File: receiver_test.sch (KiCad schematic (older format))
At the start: 9 parts, among them J1 Conn_Coaxial, J2 Conn_Coaxial, J3 Conn_01x02_Male, J4 Conn_01x02_Male, J5 Conn_01x02_Male, U1 ADE-1H+

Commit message: Nyáktervezésre majdnem kész
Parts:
- added C33: 47u, Capacitor_SMD:CP_Elec_6.3x5.3, symbol Device:CP
- added C34: 100n, Capacitor_SMD:C_0805_2012Metric_Pad1.15x1.40mm_HandSolder, symbol Device:C
- added J6: Conn_01x02_Male, Connector_PinSocket_2.54mm:PinSocket_1x02_P2.54mm_Vertical, symbol Connector:Conn_01x02_Male
- added R11: 100, Resistor_SMD:R_0805_2012Metric_Pad1.15x1.40mm_HandSolder, symbol Device:R
- added R25, R26, R27, R28, R29, R30, R31, R32, R33, R34: BP, Resistor_SMD:R_1206_3216Metric_Pad1.42x1.75mm_HandSolder, symbol Device:R
- J2: footprint (none) -> Connector_Coaxial:SMA_Molex_73251-1153_EdgeMount_Horizontal
- J3, J4, J5: footprint (none) -> Connector_PinSocket_2.54mm:PinSocket_1x02_P2.54mm_Vertical
- R1, R2, R3: footprint (none) -> Resistor_SMD:R_0805_2012Metric_Pad1.15x1.40mm_HandSolder
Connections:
- net +5VA: now also C33.1, C34.1, R11.2
- net 30MHz LPF/IN: now also R25.2; no longer J1.1 (In)
- net 30MHz LPF/OUT: now also R26.1
- net 37.4 MHz Amp, and 2nd mixer/IN: now also R28.1
- net 37.4 MHz Amp, and 2nd mixer/out_n: now also R31.2
- net 37.4 MHz Amp, and 2nd mixer/out_p: now also R30.2
- net 37.4 MHz Butterworth BPF/IN: now also R29.1; no longer U1.2 (IF)
- net Attenuator/OUT: now also R27.1; no longer U1.3 (RF)
- net GNDA: now also C33.2, C34.2, J6.2 (Pin_2)
- net Sheet5FE333A0/DC_CM: now also R33.2
- net Sheet5FE333A0/Out+: now also R32.2
- net Sheet5FE333A0/Out-: now also R34.2
- new net: J1.1 (In), R25.1
- new net: R29.2, U1.2 (IF)
- new net: R27.2, U1.3 (RF)
- new net: J6.1 (Pin_1), R11.1
- new net 37.4 MHz Butterworth BPF/OUT: R28.2
- new net Attenuator/IN: R26.2
- new net Sheet5FE333A0/In+: R30.1
- new net Sheet5FE333A0/In-: R31.1
- new net Sheet5FE3342E/DC_CM: R33.1
- new net Sheet5FE3342E/In+: R32.1
- new net Sheet5FE3342E/In-: R34.1
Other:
- note added: "Power\n"
- moved on the sheet: J5, R3

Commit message: Receiver test panel ++
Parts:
- removed J5: Conn_01x02_Male, Connector_PinSocket_2.54mm:PinSocket_1x02_P2.54mm_Vertical, symbol Connector:Conn_01x02_Male
- removed R25: BP, Resistor_SMD:R_1206_3216Metric_Pad1.42x1.75mm_HandSolder, symbol Device:R
- added C35: 10p, Capacitor_SMD:C_0805_2012Metric_Pad1.18x1.45mm_HandSolder, symbol Device:C
- added D1: Red, LED_SMD:LED_0805_2012Metric_Pad1.15x1.40mm_HandSolder, symbol Device:LED
- added H1, H2, H3, H4: 3mm spacer, MountingHole:MountingHole_3.2mm_M3, symbol Mechanical:MountingHole
- added TP1, TP10, TP2, TP3, TP4, TP5, TP6, TP7: TestPoint, Connector_PinHeader_2.54mm:PinHeader_1x01_P2.54mm_Vertical, symbol Connector:TestPoint
- added TP11, TP12, TP13, TP8, TP9: TestPoint_2Pole, Connector_PinHeader_2.54mm:PinHeader_1x02_P2.54mm_Vertical, symbol Connector:TestPoint_2Pole
- C33: symbol Device:CP -> receiver_test-rescue:CP-Device
- J1: value Conn_Coaxial -> RF_IN
- J2: value Conn_Coaxial -> IF_IN
- J6: value Conn_01x02_Male -> 5V
- R1, R2: value R -> nk
- R11: value 100 -> 470
- R3: value R -> 10k
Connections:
- net +5VA: now also J6.1 (Pin_1), R11.1; no longer R11.2
- net 30MHz LPF/IN: now also J1.1 (In)
- net 30MHz LPF/OUT: now also TP1.1
- net 37.4 MHz Amp, and 2nd mixer/IN: now also TP5.1
- net 37.4 MHz Amp, and 2nd mixer/out_n: now also TP8.2
- net 37.4 MHz Amp, and 2nd mixer/out_p: now also TP8.1
- net Attenuator/IN: now also TP2.1
- net Attenuator/OUT: now also R27.2, TP3.1; no longer R27.1
- net GNDA: now also D1.1 (K)
- net Sheet5FE333A0/DC_CM: now also R34.2; no longer R33.2
- net Sheet5FE333A0/In+: now also TP9.1
- net Sheet5FE333A0/In-: now also TP9.2
- net Sheet5FE333A0/Out+: now also TP11.1
- net Sheet5FE333A0/Out-: now also R33.2, TP11.2; no longer R34.2
- net Sheet5FE3342E/DC_CM: now also R34.1; no longer R33.1
- net Sheet5FE3342E/In+: now also TP12.1
- net Sheet5FE3342E/In-: now also R33.1, TP12.2; no longer R34.1
- net Sheet5FE3342E/Out+: now also C35.1, TP13.1
- net Sheet5FE3342E/Out-: now also C35.2, TP13.2
- net at R29.2, U1.2 (IF): now also TP6.1
- net at U1.3 (RF): now also R27.1, TP4.1; no longer R27.2
- net 37.4 MHz Butterworth BPF/IN renamed 37.4 MHz Inv-Chebysev BPF/IN
- net 37.4 MHz Inv-Chebysev BPF/IN: now also TP7.1
- net 37.4 MHz Butterworth BPF/OUT renamed 37.4 MHz Inv-Chebysev BPF/OUT
- net 37.4 MHz Inv-Chebysev BPF/OUT: now also TP10.1
- new net: D1.2 (A), R11.2
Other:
- moved on the sheet: C33, C34, J3, J4, J6, R1, R2, R26, R27, R28, R29, R3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

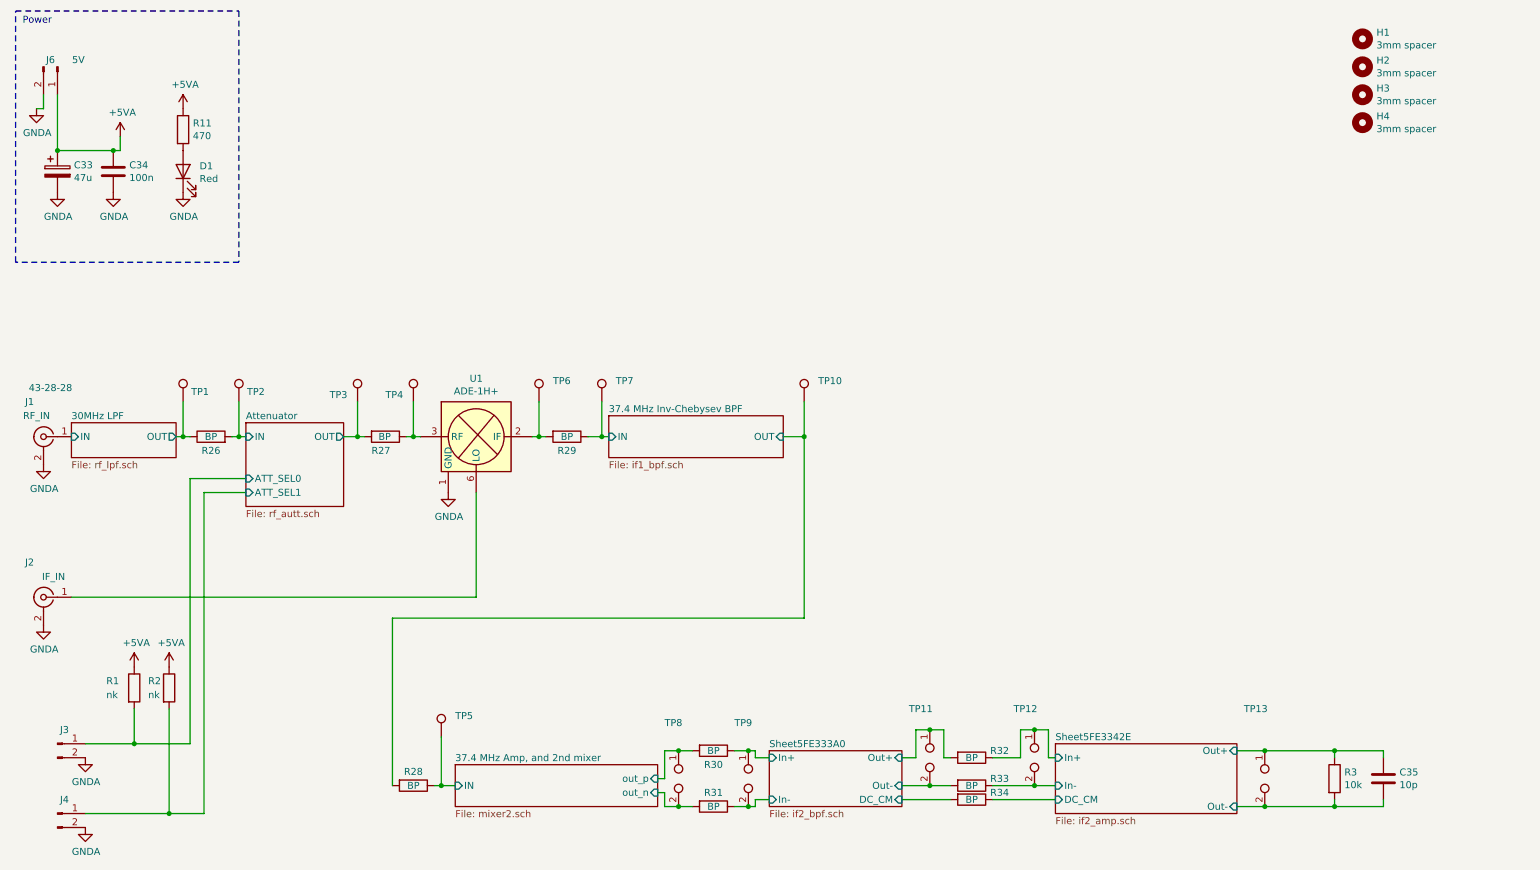
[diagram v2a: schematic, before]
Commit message: if2_bpf revised + Schematic cleanup
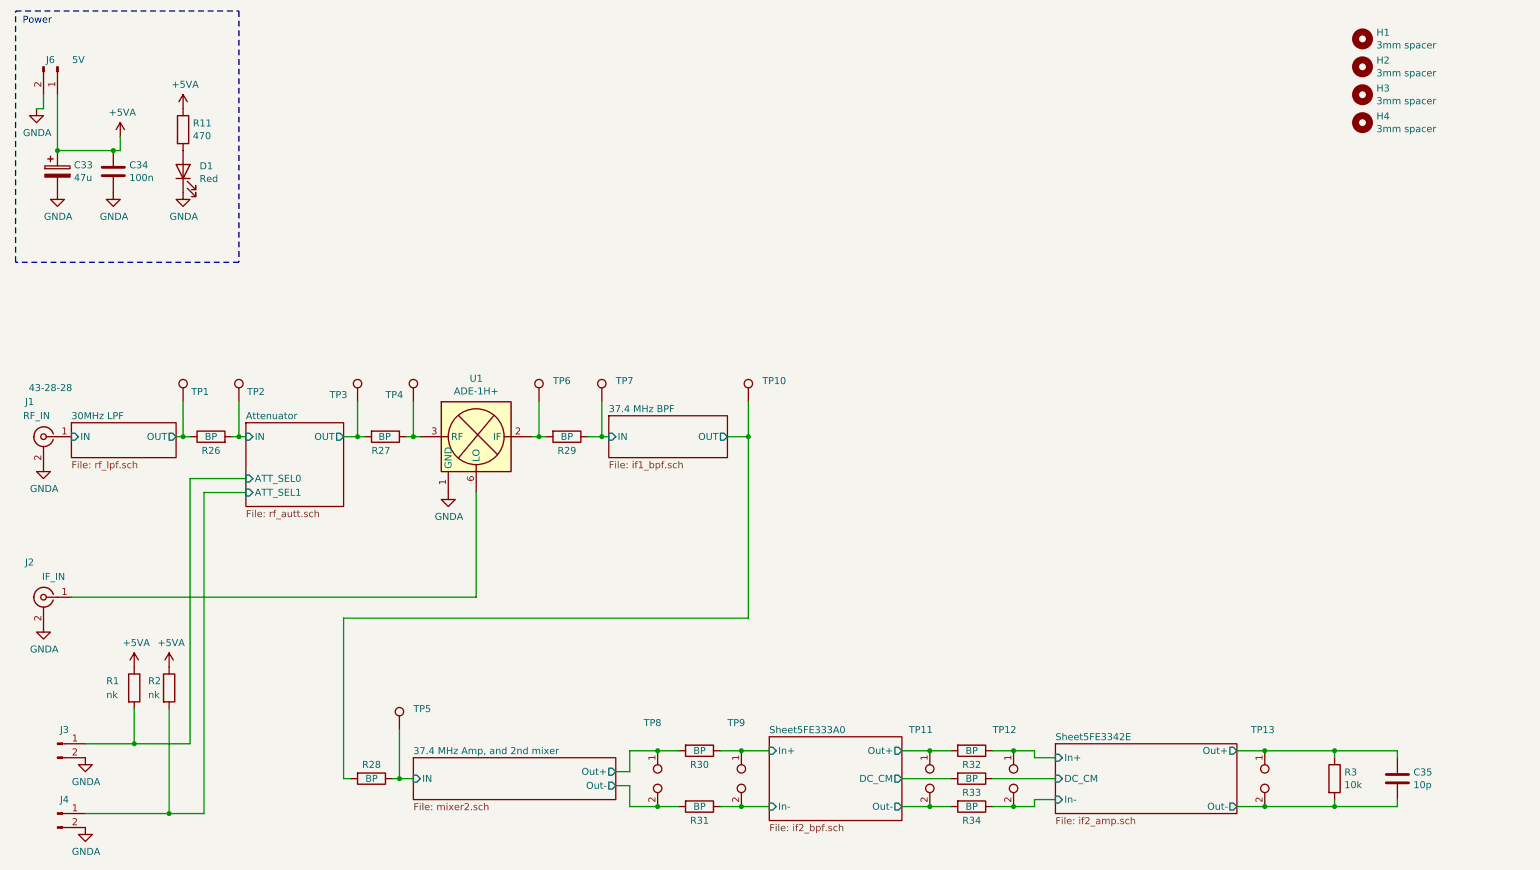
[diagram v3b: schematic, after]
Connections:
- net Sheet5FE333A0/DC_CM: now also R33.2; no longer R34.2
- net Sheet5FE333A0/Out-: now also R34.2; no longer R33.2
- net Sheet5FE3342E/DC_CM: now also R33.1; no longer R34.1
- net Sheet5FE3342E/In-: now also R34.1; no longer R33.1
- net 37.4 MHz Amp, and 2nd mixer/out_n renamed 37.4 MHz Amp, and 2nd mixer/Out-
- net 37.4 MHz Amp, and 2nd mixer/out_p renamed 37.4 MHz Amp, and 2nd mixer/Out+
- net 37.4 MHz Inv-Chebysev BPF/IN renamed 37.4 MHz BPF/IN
- net 37.4 MHz Inv-Chebysev BPF/OUT renamed 37.4 MHz BPF/OUT
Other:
- moved on the sheet: C35, R28, R30, R31, R32, R33, R34, TP10, TP11, TP12, TP5, TP8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

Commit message: Pcb vHA8KDA
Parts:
- C34: footprint Capacitor_SMD:C_0805_2012Metric_Pad1.15x1.40mm_HandSolder -> Capacitor_SMD:C_0805_2012Metric_Pad1.18x1.45mm_HandSolder
- R1, R2: value nk -> 5k; footprint Resistor_SMD:R_0805_2012Metric_Pad1.15x1.40mm_HandSolder -> Resistor_SMD:R_0805_2012Metric_Pad1.20x1.40mm_HandSolder
- R11, R3: footprint Resistor_SMD:R_0805_2012Metric_Pad1.15x1.40mm_HandSolder -> Resistor_SMD:R_0805_2012Metric_Pad1.20x1.40mm_HandSolder
- R26, R27, R28, R29, R30, R31, R32, R33, R34: footprint Resistor_SMD:R_1206_3216Metric_Pad1.42x1.75mm_HandSolder -> Resistor_SMD:R_1206_3216Metric_Pad1.30x1.75mm_HandSolder
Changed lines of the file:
@@
 F 0 "R3" H 10170 6146 50  0000 L CNN
 F 1 "10k" H 10170 6055 50  0000 L CNN
-F 2 "Resistor_SMD:R_0805_2012Metric_Pad1.15x1.40mm_HandSolder" V 10030 6100 50  0001 C CNN
+F 2 "Resistor_SMD:R_0805_2012Metric_Pad1.20x1.40mm_HandSolder" V 10030 6100 50  0001 C CNN
 F 3 "~" H 10100 6100 50  0001 C CNN
 	1    10100 6100
@@
 P 1500 5450
 F 0 "R1" H 1300 5500 50  0000 L CNN
-F 1 "nk" H 1300 5400 50  0000 L CNN
-F 2 "Resistor_SMD:R_0805_2012Metric_Pad1.15x1.40mm_HandSolder" V 1430 5450 50  0001 C CNN
+F 1 "5k" H 1300 5400 50  0000 L CNN
+F 2 "Resistor_SMD:R_0805_2012Metric_Pad1.20x1.40mm_HandSolder" V 1430 5450 50  0001 C CNN
 F 3 "~" H 1500 5450 50  0001 C CNN
 	1    1500 5450
@@
 P 1750 5450
 F 0 "R2" H 1600 5500 50  0000 L CNN
-F 1 "nk" H 1600 5400 50  0000 L CNN
-F 2 "Resistor_SMD:R_0805_2012Metric_Pad1.15x1.40mm_HandSolder" V 1680 5450 50  0001 C CNN
+F 1 "5k" H 1600 5400 50  0000 L CNN
+F 2 "Resistor_SMD:R_0805_2012Metric_Pad1.20x1.40mm_HandSolder" V 1680 5450 50  0001 C CNN
 F 3 "~" H 1750 5450 50  0001 C CNN
 	1    1750 5450
@@
 F 0 "R29" V 4700 3650 50  0000 C CNN
 F 1 "BP" V 4600 3650 50  0000 C CNN
-F 2 "Resistor_SMD:R_1206_3216Metric_Pad1.42x1.75mm_HandSolder" V 4530 3650 50  0001 C CNN
+F 2 "Resistor_SMD:R_1206_3216Metric_Pad1.30x1.75mm_HandSolder" V 4530 3650 50  0001 C CNN
 F 3 "~" H 4600 3650 50  0001 C CNN
 	1    4600 3650
@@
 F 0 "R27" V 3400 3550 50  0000 L CNN
 F 1 "BP" V 3300 3600 50  0000 L CNN
-F 2 "Resistor_SMD:R_1206_3216Metric_Pad1.42x1.75mm_HandSolder" V 3230 3650 50  0001 C CNN
+F 2 "Resistor_SMD:R_1206_3216Metric_Pad1.30x1.75mm_HandSolder" V 3230 3650 50  0001 C CNN
 F 3 "~" H 3300 3650 50  0001 C CNN
 	1    3300 3650
@@
 F 0 "R26" V 1950 3650 50  0000 C CNN
 F 1 "BP" V 2050 3650 50  0000 C CNN
-F 2 "Resistor_SMD:R_1206_3216Metric_Pad1.42x1.75mm_HandSolder" V 1980 3650 50  0001 C CNN
+F 2 "Resistor_SMD:R_1206_3216Metric_Pad1.30x1.75mm_HandSolder" V 1980 3650 50  0001 C CNN
 F 3 "~" H 2050 3650 50  0001 C CNN
 	1    2050 3650
@@
 F 0 "R28" V 3100 6100 50  0000 C CNN
 F 1 "BP" V 3200 6100 50  0000 C CNN
-F 2 "Resistor_SMD:R_1206_3216Metric_Pad1.42x1.75mm_HandSolder" V 3130 6100 50  0001 C CNN
+F 2 "Resistor_SMD:R_1206_3216Metric_Pad1.30x1.75mm_HandSolder" V 3130 6100 50  0001 C CNN
 F 3 "~" H 3200 6100 50  0001 C CNN
 	1    3200 6100
@@
 F 0 "R30" V 5650 5900 50  0000 C CNN
 F 1 "BP" V 5550 5900 50  0000 C CNN
-F 2 "Resistor_SMD:R_1206_3216Metric_Pad1.42x1.75mm_HandSolder" V 5480 5900 50  0001 C CNN
+F 2 "Resistor_SMD:R_1206_3216Metric_Pad1.30x1.75mm_HandSolder" V 5480 5900 50  0001 C CNN
 F 3 "~" H 5550 5900 50  0001 C CNN
 	1    5550 5900
@@
 F 0 "R31" V 5650 6300 50  0000 C CNN
 F 1 "BP" V 5550 6300 50  0000 C CNN
-F 2 "Resistor_SMD:R_1206_3216Metric_Pad1.42x1.75mm_HandSolder" V 5480 6300 50  0001 C CNN
+F 2 "Resistor_SMD:R_1206_3216Metric_Pad1.30x1.75mm_HandSolder" V 5480 6300 50  0001 C CNN
 F 3 "~" H 5550 6300 50  0001 C CNN
 	1    5550 6300
@@
 F 0 "C34" H 1465 1796 50  0000 L CNN
 F 1 "100n" H 1465 1705 50  0000 L CNN
-F 2 "Capacitor_SMD:C_0805_2012Metric_Pad1.15x1.40mm_HandSolder" H 1388 1600 50  0001 C CNN
+F 2 "Capacitor_SMD:C_0805_2012Metric_Pad1.18x1.45mm_HandSolder" H 1388 1600 50  0001 C CNN
 F 3 "~" H 1350 1750 50  0001 C CNN
 	1    1350 1750
@@
 F 0 "R11" H 1920 1496 50  0000 L CNN
 F 1 "470" H 1920 1405 50  0000 L CNN
-F 2 "Resistor_SMD:R_0805_2012Metric_Pad1.15x1.40mm_HandSolder" V 1780 1450 50  0001 C CNN
+F 2 "Resistor_SMD:R_0805_2012Metric_Pad1.20x1.40mm_HandSolder" V 1780 1450 50  0001 C CNN
 F 3 "~" H 1850 1450 50  0001 C CNN
 	1    1850 1450
@@
 F 0 "R34" V 7600 6300 50  0000 C CNN
 F 1 "BP" V 7500 6300 50  0000 C CNN
-F 2 "Resistor_SMD:R_1206_3216Metric_Pad1.42x1.75mm_HandSolder" V 7430 6300 50  0001 C CNN
+F 2 "Resistor_SMD:R_1206_3216Metric_Pad1.30x1.75mm_HandSolder" V 7430 6300 50  0001 C CNN
 F 3 "~" H 7500 6300 50  0001 C CNN
 	1    7500 6300
@@
 F 0 "R33" V 7600 6100 50  0000 C CNN
 F 1 "BP" V 7500 6100 50  0000 C CNN
-F 2 "Resistor_SMD:R_1206_3216Metric_Pad1.42x1.75mm_HandSolder" V 7430 6100 50  0001 C CNN
+F 2 "Resistor_SMD:R_1206_3216Metric_Pad1.30x1.75mm_HandSolder" V 7430 6100 50  0001 C CNN
 F 3 "~" H 7500 6100 50  0001 C CNN
 	1    7500 6100
@@
 F 0 "R32" V 7600 5900 50  0000 C CNN
 F 1 "BP" V 7500 5900 50  0000 C CNN
-F 2 "Resistor_SMD:R_1206_3216Metric_Pad1.42x1.75mm_HandSolder" V 7430 5900 50  0001 C CNN
+F 2 "Resistor_SMD:R_1206_3216Metric_Pad1.30x1.75mm_HandSolder" V 7430 5900 50  0001 C CNN
 F 3 "~" H 7500 5900 50  0001 C CNN
 	1    7500 5900

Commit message: Pcb edges and spacer part number
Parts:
- H1: Lomex (none) -> 14-00-89 + 14-01-46
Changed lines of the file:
@@
 F 2 "MountingHole:MountingHole_3.2mm_M3" H 10300 800 50  0001 C CNN
 F 3 "~" H 10300 800 50  0001 C CNN
+F 4 "14-00-89 + 14-01-46" H 10300 800 50  0001 C CNN "Lomex"
 	1    10300 800
 	1    0    0    -1

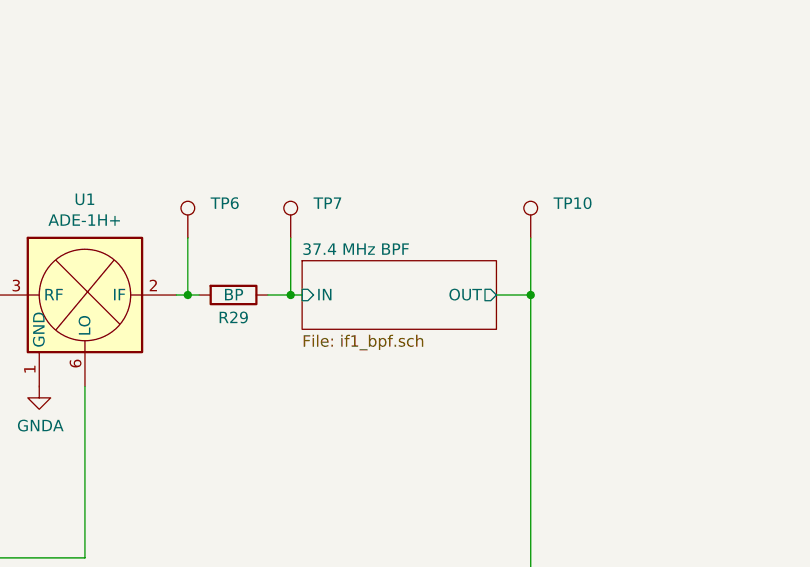
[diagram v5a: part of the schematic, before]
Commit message: IF1 modified to 37,224 MHz
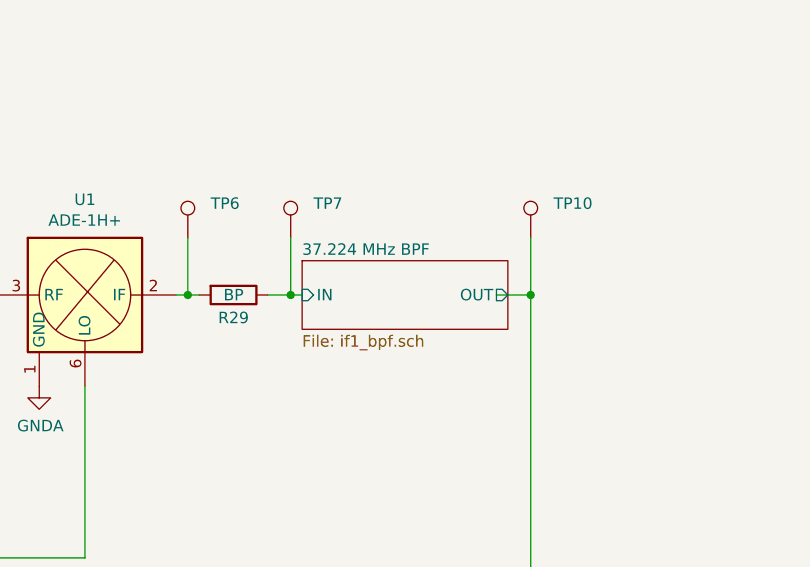
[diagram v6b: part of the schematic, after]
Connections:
- net 37.4 MHz BPF/IN renamed 37.224 MHz BPF/IN
- net 37.4 MHz BPF/OUT: no longer names the net of R28.2, TP10.1
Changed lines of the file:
@@
 $EndSheet
 $Sheet
-S 4900 3500 850  300
+S 4900 3500 900  300
 U 5FE33197
-F0 "37.4 MHz BPF" 50
+F0 "37.224 MHz BPF" 50
 F1 "if1_bpf.sch" 50
 F2 "IN" I L 4900 3650 50
-F3 "OUT" O R 5750 3650 50
+F3 "OUT" O R 5800 3650 50
 $EndSheet
 $Sheet

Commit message: RX PCB revision: Diff amp + Mixer2
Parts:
- removed C35: 10p, Capacitor_SMD:C_0805_2012Metric_Pad1.18x1.45mm_HandSolder, symbol Device:C
- removed R3: 10k, Resistor_SMD:R_0805_2012Metric_Pad1.20x1.40mm_HandSolder, symbol Device:R
- removed R32, R33, R34: BP, Resistor_SMD:R_1206_3216Metric_Pad1.30x1.75mm_HandSolder, symbol Device:R
- removed TP11, TP13: TestPoint_2Pole, Connector_PinHeader_2.54mm:PinHeader_1x02_P2.54mm_Vertical, symbol Connector:TestPoint_2Pole
- C2: renamed from C34; footprint Capacitor_SMD:C_0805_2012Metric_Pad1.18x1.45mm_HandSolder -> Capacitor_SMD:C_0805_2012Metric_Pad1.15x1.40mm_HandSolder
- R1: renamed from R11; footprint Resistor_SMD:R_0805_2012Metric_Pad1.20x1.40mm_HandSolder -> Resistor_SMD:R_0805_2012Metric_Pad1.15x1.40mm_HandSolder
- R2: renamed from R26; footprint Resistor_SMD:R_1206_3216Metric_Pad1.30x1.75mm_HandSolder -> Resistor_SMD:R_1206_3216Metric_Pad1.42x1.75mm_HandSolder
- R3: renamed from R27; footprint Resistor_SMD:R_1206_3216Metric_Pad1.30x1.75mm_HandSolder -> Resistor_SMD:R_1206_3216Metric_Pad1.42x1.75mm_HandSolder
- R4: renamed from R29; footprint Resistor_SMD:R_1206_3216Metric_Pad1.30x1.75mm_HandSolder -> Resistor_SMD:R_1206_3216Metric_Pad1.42x1.75mm_HandSolder
- R5: renamed from R1; footprint Resistor_SMD:R_0805_2012Metric_Pad1.20x1.40mm_HandSolder -> Resistor_SMD:R_0805_2012Metric_Pad1.15x1.40mm_HandSolder
- R6: renamed from R2; footprint Resistor_SMD:R_0805_2012Metric_Pad1.20x1.40mm_HandSolder -> Resistor_SMD:R_0805_2012Metric_Pad1.15x1.40mm_HandSolder
- R7: renamed from R30; footprint Resistor_SMD:R_1206_3216Metric_Pad1.30x1.75mm_HandSolder -> Resistor_SMD:R_1206_3216Metric_Pad1.42x1.75mm_HandSolder
- R8: renamed from R28; footprint Resistor_SMD:R_1206_3216Metric_Pad1.30x1.75mm_HandSolder -> Resistor_SMD:R_1206_3216Metric_Pad1.42x1.75mm_HandSolder
- R9: renamed from R31; footprint Resistor_SMD:R_1206_3216Metric_Pad1.30x1.75mm_HandSolder -> Resistor_SMD:R_1206_3216Metric_Pad1.42x1.75mm_HandSolder
- renumbered C33 to C1, J6 to J1, J1 to J2, J2 to J3, J3 to J4, J4 to J5, TP9 to TP10, TP12 to TP11, TP6 to TP5, TP7 to TP6, TP10 to TP7, TP5 to TP8, TP8 to TP9
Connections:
- net Sheet5FE3342E/In+ is gone; now on net Sheet5FE333A0/Out+: TP11.1
- net Sheet5FE3342E/In- is gone; now on net Sheet5FE333A0/Out-: TP11.2
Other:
- note added: "Szimulált terhelés(ek)\naz if2_amp lapon"
- moved on the sheet: TP11
